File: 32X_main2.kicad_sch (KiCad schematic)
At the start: 54 parts, among them IC501 SH2 M, IC502 SH2 S, IC503 uPD4502161, IC504 315-5818, IC506 315-5781, IC507 TC511664, IC508 TC511664, IC509 74AC04, IC510 RHSRL33A

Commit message: Enlarge some footprints, fix unwanted A/D ground connections.
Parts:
- IC509: footprint Package_SO:SO-14_3.9x8.65mm_P1.27mm -> Package_SO:SO-14_5.3x10.2mm_P1.27mm
- L501: footprint Inductor_SMD:L_0805_2012Metric -> Inductor_SMD:L_1206_3216Metric
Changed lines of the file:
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@@
       (effects (font (size 1.27 1.27)))
     )
-    (property "Footprint" "Package_SO:SO-14_3.9x8.65mm_P1.27mm" (at 377.19 232.41 0)
+    (property "Footprint" "Package_SO:SO-14_5.3x10.2mm_P1.27mm" (at 377.19 232.41 0)
       (effects (font (size 1.27 1.27)) hide)
     )
@@
       (effects (font (size 1.27 1.27)) (justify left))
     )
-    (property "Footprint" "Inductor_SMD:L_0805_2012Metric" (at 223.52 243.84 0)
+    (property "Footprint" "Inductor_SMD:L_1206_3216Metric" (at 223.52 243.84 0)
       (effects (font (size 1.27 1.27)) hide)
     )
@@
       (effects (font (size 1.27 1.27)))
     )
-    (property "Footprint" "Package_SO:SO-14_3.9x8.65mm_P1.27mm" (at 340.995 232.41 0)
-      (effects (font (size 1.27 1.27)) hide)
-    )
+    (property "Footprint" "Package_SO:SO-14_5.3x10.2mm_P1.27mm" (at 340.995 232.41 0)
+      (effects (font (size 1.27 1.27)) hide)
+    )

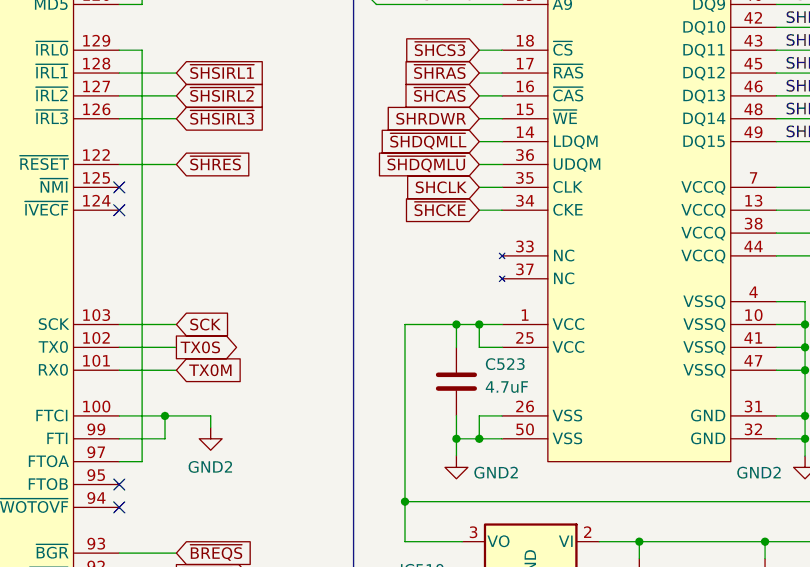
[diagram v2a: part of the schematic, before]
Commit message: Add/correct MD PAL timing caps.
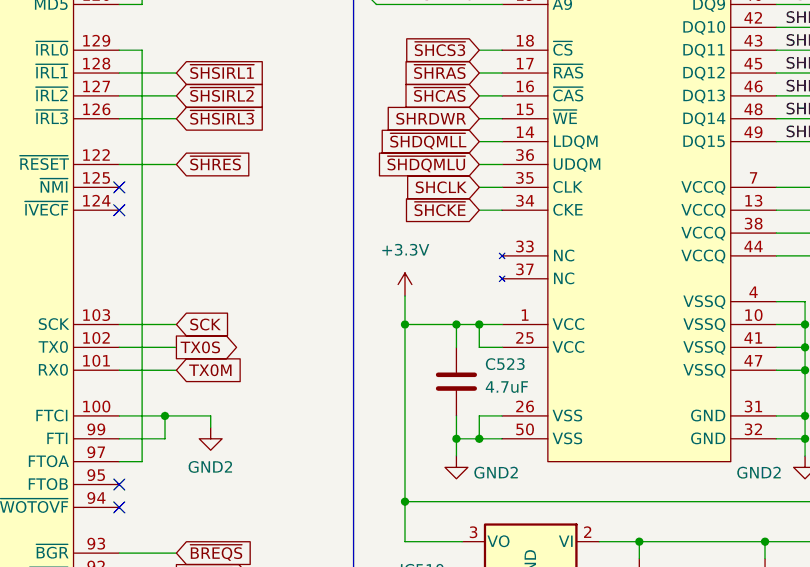
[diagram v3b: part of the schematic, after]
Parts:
- renumbered C522 to C521, C521 to C522
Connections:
- net +3.3V: now reaches C523.1, IC503.1 (VCC), IC503.13 (VCCQ), IC503.25 (VCC), IC503.38 (VCCQ), IC503.44 (VCCQ), IC503.7 (VCCQ), IC510.3 (VO)
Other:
- moved on the sheet: C521, C522
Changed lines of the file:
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@@
   (junction (at 66.675 212.725) (diameter 0) (color 0 0 0 0)
   )
+  (junction (at 166.37 88.265) (diameter 0) (color 0 0 0 0)
+  )
   (junction (at 206.375 112.395) (diameter 0) (color 0 0 0 0)
   )
@@
     (stroke (width 0) (type default))
   )
+  (wire (pts (xy 166.37 85.09) (xy 166.37 88.265))
+    (stroke (width 0) (type default))
+  )
   (wire (pts (xy 163.195 52.705) (xy 177.165 52.705))
     (stroke (width 0) (type default))
@@
     )
   )
-  (symbol (lib_id "Device:C") (at 206.375 118.11 0) (mirror y) (unit 1)
+  (symbol (lib_id "Device:C") (at 219.71 118.11 0) (mirror y) (unit 1)
     (in_bom yes) (on_board yes) (dnp no)
-    (property "Reference" "C521" (at 210.185 116.205 0)
+    (property "Reference" "C522" (at 223.52 116.205 0)
       (effects (font (size 1.27 1.27)) (justify right))
     )
-    (property "Value" "100nF" (at 210.185 118.745 0)
+    (property "Value" "100nF" (at 223.52 118.745 0)
       (effects (font (size 1.27 1.27)) (justify right))
     )
-    (property "Footprint" "Capacitor_SMD:C_0805_2012Metric" (at 205.4098 121.92 0)
+    (property "Footprint" "Capacitor_SMD:C_0805_2012Metric" (at 218.7448 121.92 0)
       (effects (font (size 1.27 1.27)) hide)
     )
-    (property "Datasheet" "~" (at 206.375 118.11 0)
+    (property "Datasheet" "~" (at 219.71 118.11 0)
       (effects (font (size 1.27 1.27)) hide)
     )
-    (property "DigiKey" "" (at 206.375 118.11 0)
+    (property "DigiKey" "" (at 219.71 118.11 0)
       (effects (font (size 1.27 1.27)) hide)
     )
@@
       (project "Neptune"
         (path "/bcc23b51-b742-4ae5-9dd6-d96a24058944/e4c57f96-d802-4292-9df6-7ff62ef14a9e"
-          (reference "C521") (unit 1)
+          (reference "C522") (unit 1)
         )
       )
@@
     )
   )
-  (symbol (lib_id "Device:C") (at 219.71 118.11 0) (mirror y) (unit 1)
+  (symbol (lib_id "Device:C") (at 206.375 118.11 0) (mirror y) (unit 1)
     (in_bom yes) (on_board yes) (dnp no)
-    (property "Reference" "C522" (at 223.52 116.205 0)
+    (property "Reference" "C521" (at 210.185 116.205 0)
       (effects (font (size 1.27 1.27)) (justify right))
     )
-    (property "Value" "100nF" (at 223.52 118.745 0)
+    (property "Value" "100nF" (at 210.185 118.745 0)
       (effects (font (size 1.27 1.27)) (justify right))
     )
-    (property "Footprint" "Capacitor_SMD:C_0805_2012Metric" (at 218.7448 121.92 0)
+    (property "Footprint" "Capacitor_SMD:C_0805_2012Metric" (at 205.4098 121.92 0)
       (effects (font (size 1.27 1.27)) hide)
     )
-    (property "Datasheet" "~" (at 219.71 118.11 0)
+    (property "Datasheet" "~" (at 206.375 118.11 0)
       (effects (font (size 1.27 1.27)) hide)
     )
-    (property "DigiKey" "" (at 219.71 118.11 0)
+    (property "DigiKey" "" (at 206.375 118.11 0)
       (effects (font (size 1.27 1.27)) hide)
     )
@@
       (project "Neptune"
         (path "/bcc23b51-b742-4ae5-9dd6-d96a24058944/e4c57f96-d802-4292-9df6-7ff62ef14a9e"
-          (reference "C522") (unit 1)
+          (reference "C521") (unit 1)
+        )
+      )
+    )
+  )
+  (symbol (lib_id "power:+3.3V") (at 166.37 85.09 0) (unit 1)
+    (in_bom yes) (on_board yes) (dnp no) (fields_autoplaced)
+    (property "Reference" "#PWR094" (at 166.37 88.9 0)
+      (effects (font (size 1.27 1.27)) hide)
+    )
+    (property "Value" "+3.3V" (at 166.37 80.01 0)
+      (effects (font (size 1.27 1.27)))
+    )
+    (property "Footprint" "" (at 166.37 85.09 0)
+      (effects (font (size 1.27 1.27)) hide)
+    )
+    (property "Datasheet" "" (at 166.37 85.09 0)
+      (effects (font (size 1.27 1.27)) hide)
+    )
+    (pin "1")
+    (instances
+      (project "Neptune"
+        (path "/bcc23b51-b742-4ae5-9dd6-d96a24058944/e4c57f96-d802-4292-9df6-7ff62ef14a9e"
+          (reference "#PWR094") (unit 1)
         )
       )

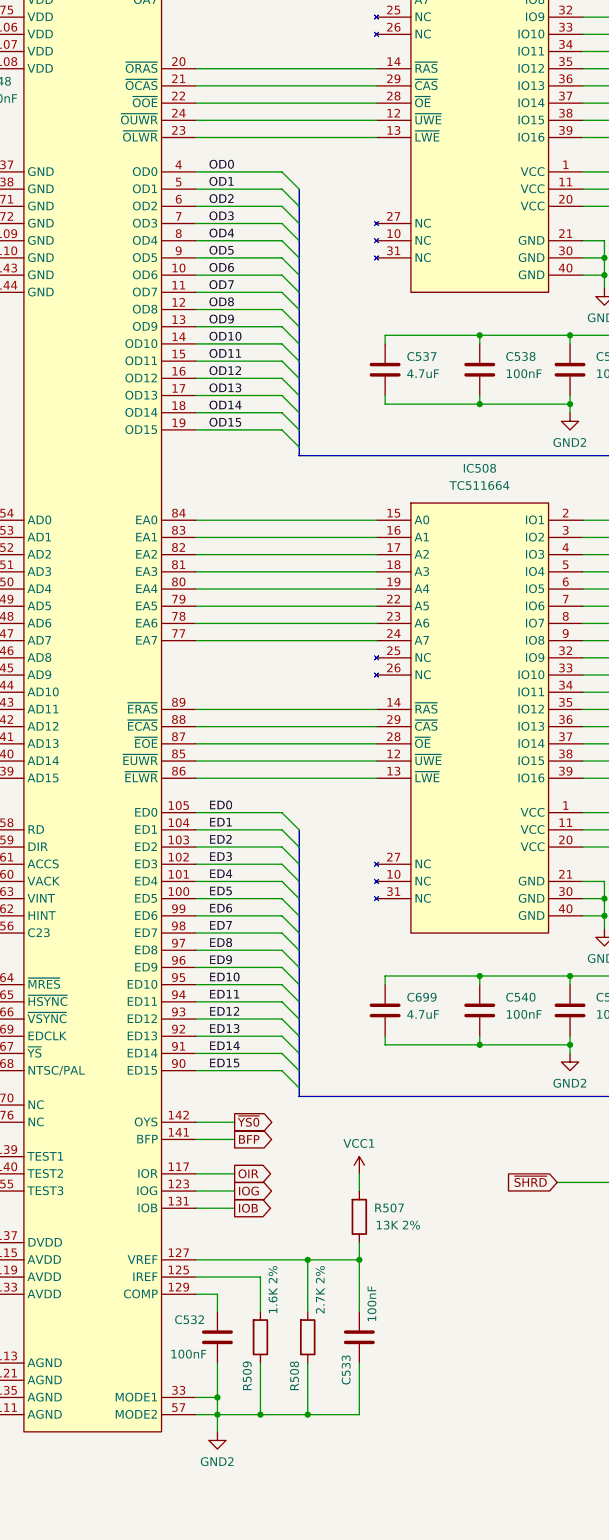
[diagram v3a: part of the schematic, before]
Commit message: Spec resistors for RGB LPF to avoid accidental short.
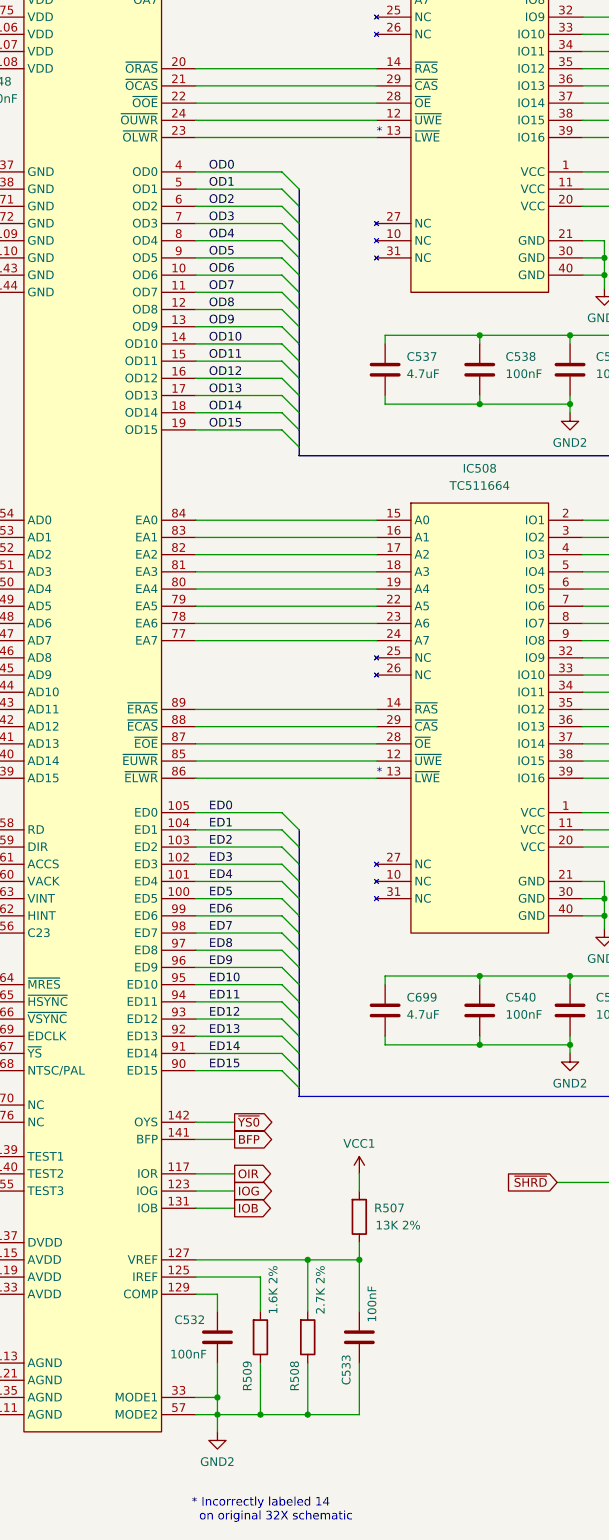
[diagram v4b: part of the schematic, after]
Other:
- note added: "*"
- note added: "* Incorrectly labeled 14 on original 32X schematic"
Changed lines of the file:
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@@
+    (effects (font (size 1.27 1.27)) (justify left bottom))
+  )
+  (text "* Incorrectly labeled 14\n  on original 32X schematic"
+    (at 269.24 282.575 0)
     (effects (font (size 1.27 1.27)) (justify left bottom))
   )
   (text "VA1 ONLY" (at 59.69 262.255 0)
     (effects (font (size 2.54 2.54)) (justify left bottom))
+  )
+  (text "*" (at 296.545 78.105 0)
+    (effects (font (size 1.27 1.27)) (justify left bottom))
   )
   (text "IC502 Part No." (at 57.15 266.7 0)
@@
     (effects (font (size 1.27 1.27)) (justify left bottom))
   )
+  (text "*" (at 296.545 172.72 0)
+    (effects (font (size 1.27 1.27)) (justify left bottom))
+  )

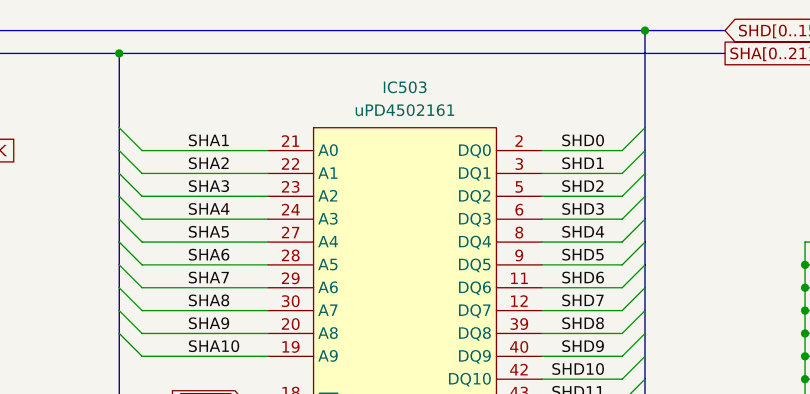
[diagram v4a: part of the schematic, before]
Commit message: Footprint improvements, general tidying.
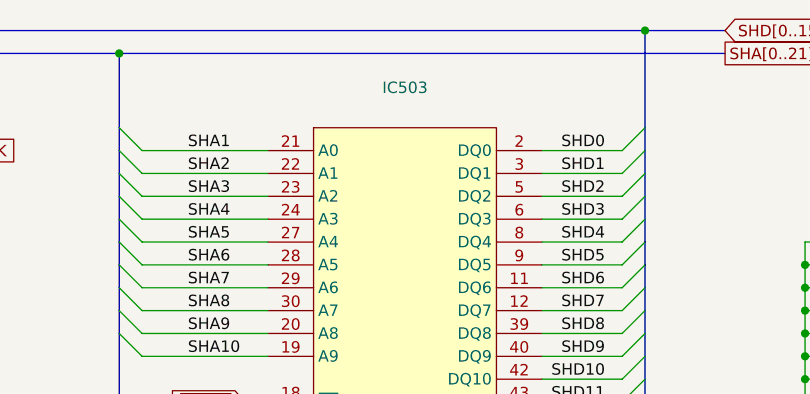
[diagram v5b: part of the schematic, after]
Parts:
- IC501, IC502, IC506: footprint Package_QFP:LQFP-144_20x20mm_P0.5mm -> Neptune:LQFP-144_20x20mm_P0.5mm
- IC503: value uPD4502161 -> µPD4502161
- IC504: footprint Package_QFP:LQFP-176_24x24mm_P0.5mm -> Neptune:LQFP-176_24x24mm_P0.5mm
- L501: footprint Inductor_SMD:L_1206_3216Metric -> Inductor_SMD:L_1210_3225Metric_Pad1.42x2.65mm_HandSolder
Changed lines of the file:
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@@
       (effects (font (size 1.27 1.27)))
     )
-    (property "Footprint" "Package_QFP:LQFP-144_20x20mm_P0.5mm" (at 48.895 62.865 0)
+    (property "Footprint" "Neptune:LQFP-144_20x20mm_P0.5mm" (at 48.895 62.865 0)
       (effects (font (size 1.27 1.27)) hide)
     )
@@
       (effects (font (size 1.27 1.27)))
     )
-    (property "Footprint" "Package_QFP:LQFP-144_20x20mm_P0.5mm" (at 119.38 62.865 0)
+    (property "Footprint" "Neptune:LQFP-144_20x20mm_P0.5mm" (at 119.38 62.865 0)
       (effects (font (size 1.27 1.27)) hide)
     )
@@
       (effects (font (size 1.27 1.27)))
     )
-    (property "Value" "uPD4502161" (at 192.405 25.4 0)
-      (effects (font (size 1.27 1.27)))
+    (property "Value" "µPD4502161" (at 192.405 25.4 0)
+      (effects (font (size 1.27 1.27)) hide)
     )
     (property "Footprint" "Neptune:SSOP-50" (at 192.405 62.865 0)
@@
       (effects (font (size 1.27 1.27)) (justify left))
     )
-    (property "Footprint" "Inductor_SMD:L_1206_3216Metric" (at 223.52 243.84 0)
+    (property "Footprint" "Inductor_SMD:L_1210_3225Metric_Pad1.42x2.65mm_HandSolder" (at 223.52 243.84 0)
       (effects (font (size 1.27 1.27)) hide)
     )
@@
       (effects (font (size 1.27 1.27)))
     )
-    (property "Footprint" "Package_QFP:LQFP-144_20x20mm_P0.5mm" (at 254.635 73.025 0)
+    (property "Footprint" "Neptune:LQFP-144_20x20mm_P0.5mm" (at 254.635 73.025 0)
       (effects (font (size 1.27 1.27)) hide)
     )
@@
       (effects (font (size 1.27 1.27)))
     )
-    (property "Footprint" "Package_QFP:LQFP-176_24x24mm_P0.5mm" (at 192.405 132.08 0)
-      (effects (font (size 1.27 1.27)) hide)
-    )
+    (property "Footprint" "Neptune:LQFP-176_24x24mm_P0.5mm" (at 192.405 132.08 0)
+      (effects (font (size 1.27 1.27)) hide)
+    )

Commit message: Added LCSC Part # for some of the bird seed
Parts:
- C5, C513, C516, C518, C519, C521, C522, C528, C531, C532, C533, C535, C536, C538, C539, C540, C541, C548: LCSC Part # (none) -> C2237864
- C511, C514: LCSC Part # (none) -> C2232577
- C512, C515, C517, C520, C523, C527, C530, C534, C537, C699: LCSC Part # (none) -> C2182015
- C525: LCSC Part # (none) -> C3842272
- C526, C696, C697: LCSC Part # (none) -> C2232364
- R502: LCSC Part # (none) -> C844937
- R503, R505: LCSC Part # (none) -> C844841
- R506: LCSC Part # (none) -> C2077041
- R507: LCSC Part # (none) -> C844395
- R508: LCSC Part # (none) -> C844836
- R509: LCSC Part # (none) -> C2077359

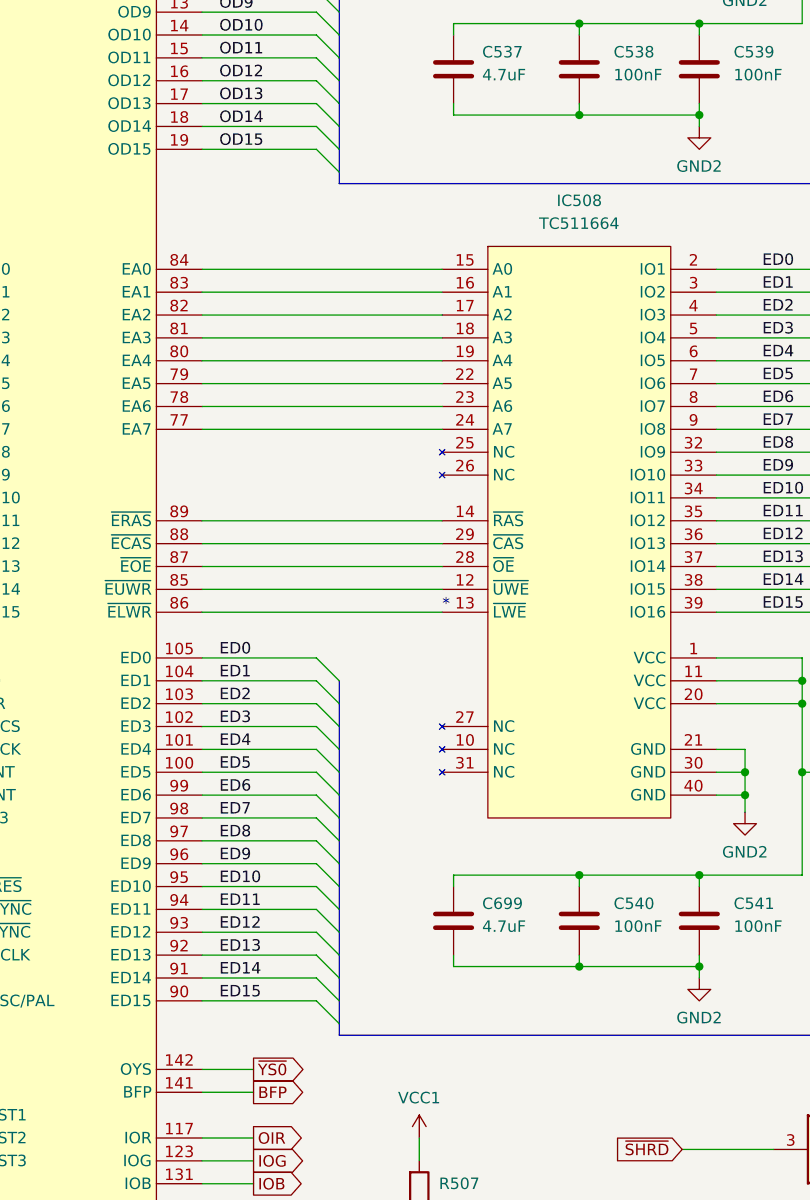
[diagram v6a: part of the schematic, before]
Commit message: Rev 1.1b
Bridged C576, not to be populated.

Fixing schematic ERC and update the PCB
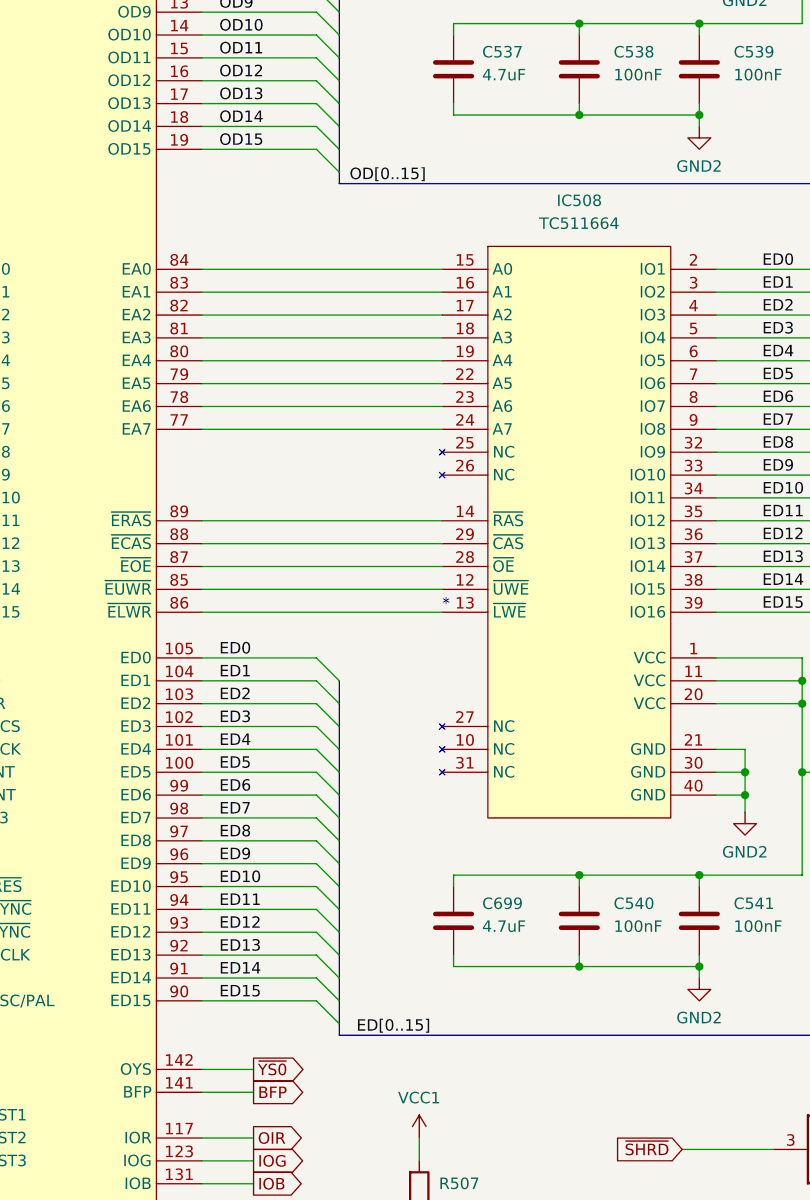
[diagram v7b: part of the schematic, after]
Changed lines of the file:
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@@
     (title "32X Main 2")
     (date "2023-11-29")
-    (rev "1.1")
+    (rev "1.1b")
     (company "By Cosam")
     (comment 1 "Neptune")
@@
     (effects (font (size 1.27 1.27)) (justify left bottom))
   )
+  (label "OD[0..15]" (at 286.258 125.095 0) (fields_autoplaced)
+    (effects (font (size 1.27 1.27)) (justify left bottom))
+  )
   (label "SHD12" (at 168.275 210.82 0) (fields_autoplaced)
     (effects (font (size 1.27 1.27)) (justify left bottom))
@@
     (effects (font (size 1.27 1.27)) (justify left bottom))
   )
+  (label "ED[0..15]" (at 287.02 219.71 0) (fields_autoplaced)
+    (effects (font (size 1.27 1.27)) (justify left bottom))
+  )

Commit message: Added more JLC Part numbers
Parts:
- IC509: LCSC Part # (none) -> C352940
- L501: LCSC Part # (none) -> C27775
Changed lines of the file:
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@@
       (effects (font (size 1.27 1.27)) hide)
     )
-    (property "LCSC Part #" "" (at 377.19 232.41 0)
+    (property "LCSC Part #" "C352940" (at 377.19 232.41 0)
       (effects (font (size 1.27 1.27)) hide)
     )
@@
       (effects (font (size 1.27 1.27)) hide)
     )
-    (property "LCSC Part #" "" (at 223.52 243.84 0)
+    (property "LCSC Part #" "C27775" (at 223.52 243.84 0)
       (effects (font (size 1.27 1.27)) hide)
     )
@@
       (effects (font (size 1.27 1.27)) hide)
     )
-    (property "LCSC Part #" "" (at 340.995 232.41 0)
-      (effects (font (size 1.27 1.27)) hide)
-    )
+    (property "LCSC Part #" "C352940" (at 340.995 232.41 0)
+      (effects (font (size 1.27 1.27)) hide)
+    )
